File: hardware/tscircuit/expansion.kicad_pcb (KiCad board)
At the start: 2 copper layers, 80 x 60 mm, 13 parts

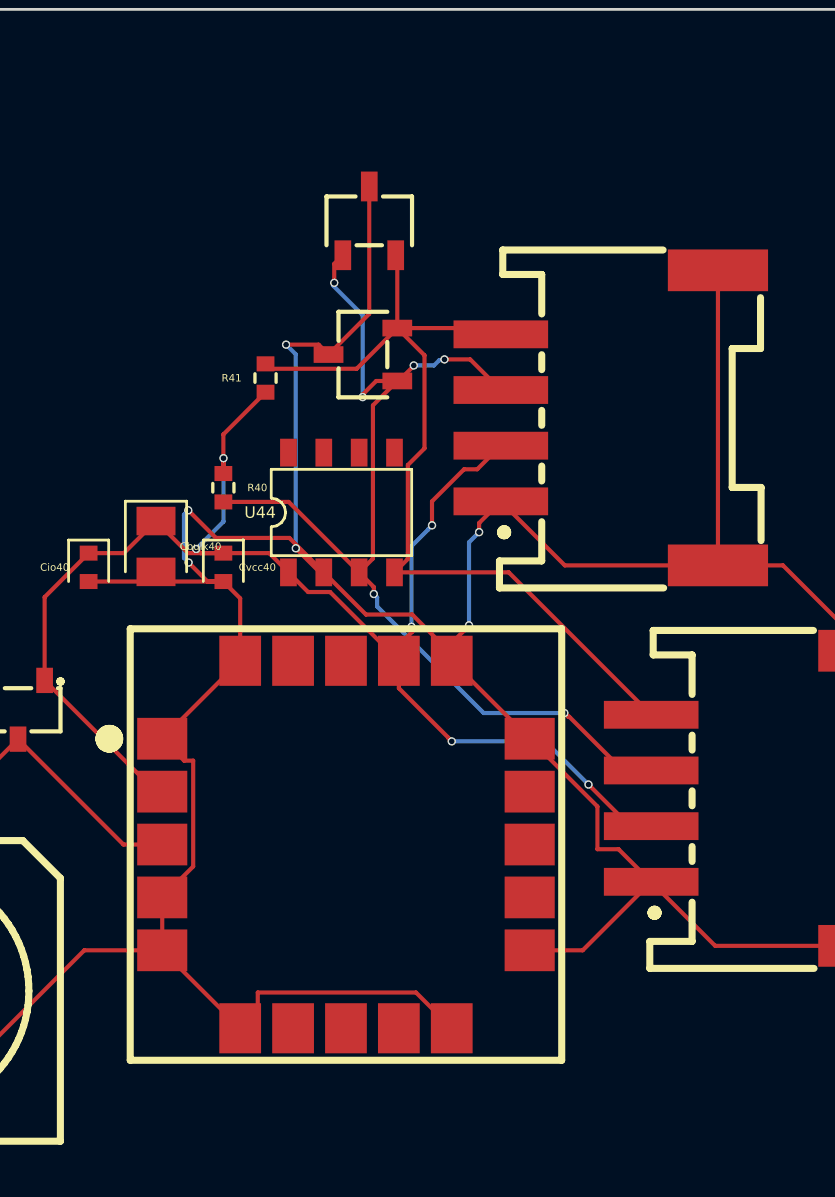
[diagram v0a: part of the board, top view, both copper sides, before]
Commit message: hw: fix 6 issues from realized-board self-review (2 blockers)
Adversarial multi-agent review of the real-parts board caught 6 real defects the
per-sheet DRC couldn't see; all datasheet-verified, fixed, sheets re-verified
(DRC parity=0 each):

- BLOCKER (power): BQ25887 SNS was tied to BAT externally -> shorts the internal
  charge-current shunt, defeating ICHG regulation on the 2S pack. SNS is now its own
  net (44uF to GND only); the SNS<->BAT shunt is internal.
- BLOCKER (expansion): PESD5V0S2UAT ESD arrays (common-cathode) had the common cathode
  on GND -> every I2C logic-high forward-biases the diode and clamps SDA/SCL to ~0.6V
  (whole bus dead). Cathode moved to +3V3 (clamps overshoot above the rail).
- MAJOR (audio): PAM8302 inputs were DC-coupled (IN- hard to GND) -> breaks the
  internal VDD/2 bias and rails the output. Added series 0.1uF caps on both inputs.
- MINOR (power): BQ25887 TS divider was missing RT2 (30.1k || NTC) -> shifted temp
  window; added.
- MINOR (power): MP2315 bootstraps were missing the datasheet-required 20R series
  resistor; added Rbst4/Rbst5.
- MINOR (rf): SP4T pins 1/8/11/12/14 are N/C per the SKY13414 datasheet -> untied from
  GND (only the EP paddle is ground).

GPIO45 (VDD_SPI strap on CC1101 GDO2) is handled by the set_flash_voltage eFuse (a
verifier false-positive) -> documented inline. Docs (power EN+RU) corrected.

Co-Authored-By: Claude Opus 4.8 <noreply@anthropic.com>
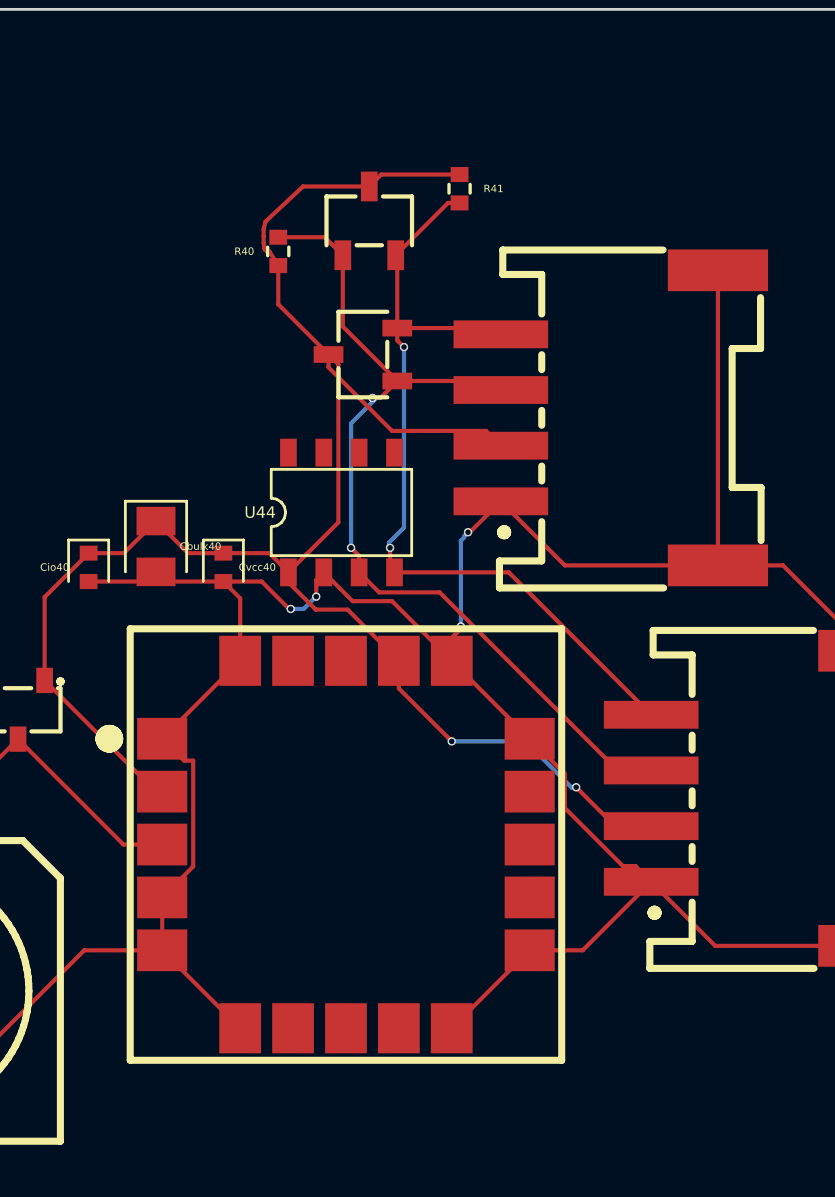
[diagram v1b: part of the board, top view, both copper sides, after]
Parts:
- moved R41 9.74 mm to (104.1, 76.4), turned to -90 degrees
- moved R40 8.71 mm to (97.6, 78.7), turned to 90 degrees
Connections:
- D40 pad 3: GND -> V3V3
- D41 pad 3: GND -> V3V3
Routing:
- net GND: track 136.0 -> 109.1 mm, vias 6 -> 4
- net V3V3: track 55.3 -> 67.1 mm, vias 6 -> 2
- net I2C_SDA: track 38.9 -> 33.1 mm, vias 6 -> 2
- net I2C_SCL: track 32.8 -> 30.0 mm, vias 0 -> 2
